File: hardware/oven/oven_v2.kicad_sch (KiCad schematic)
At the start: 21 parts, among them J1 NEUTRAL, J10 SERIAL, J2 5V_IN, J3 RELAY_PWR, J4 LIVE, J5 OUTPUT, J6 RELAY_CTRL, J7 DISPLAY, J8 NUMPAD, J9 AVR-ISP-6, U1 ATmega328-AU, U2 MAX6675, Y1 16M

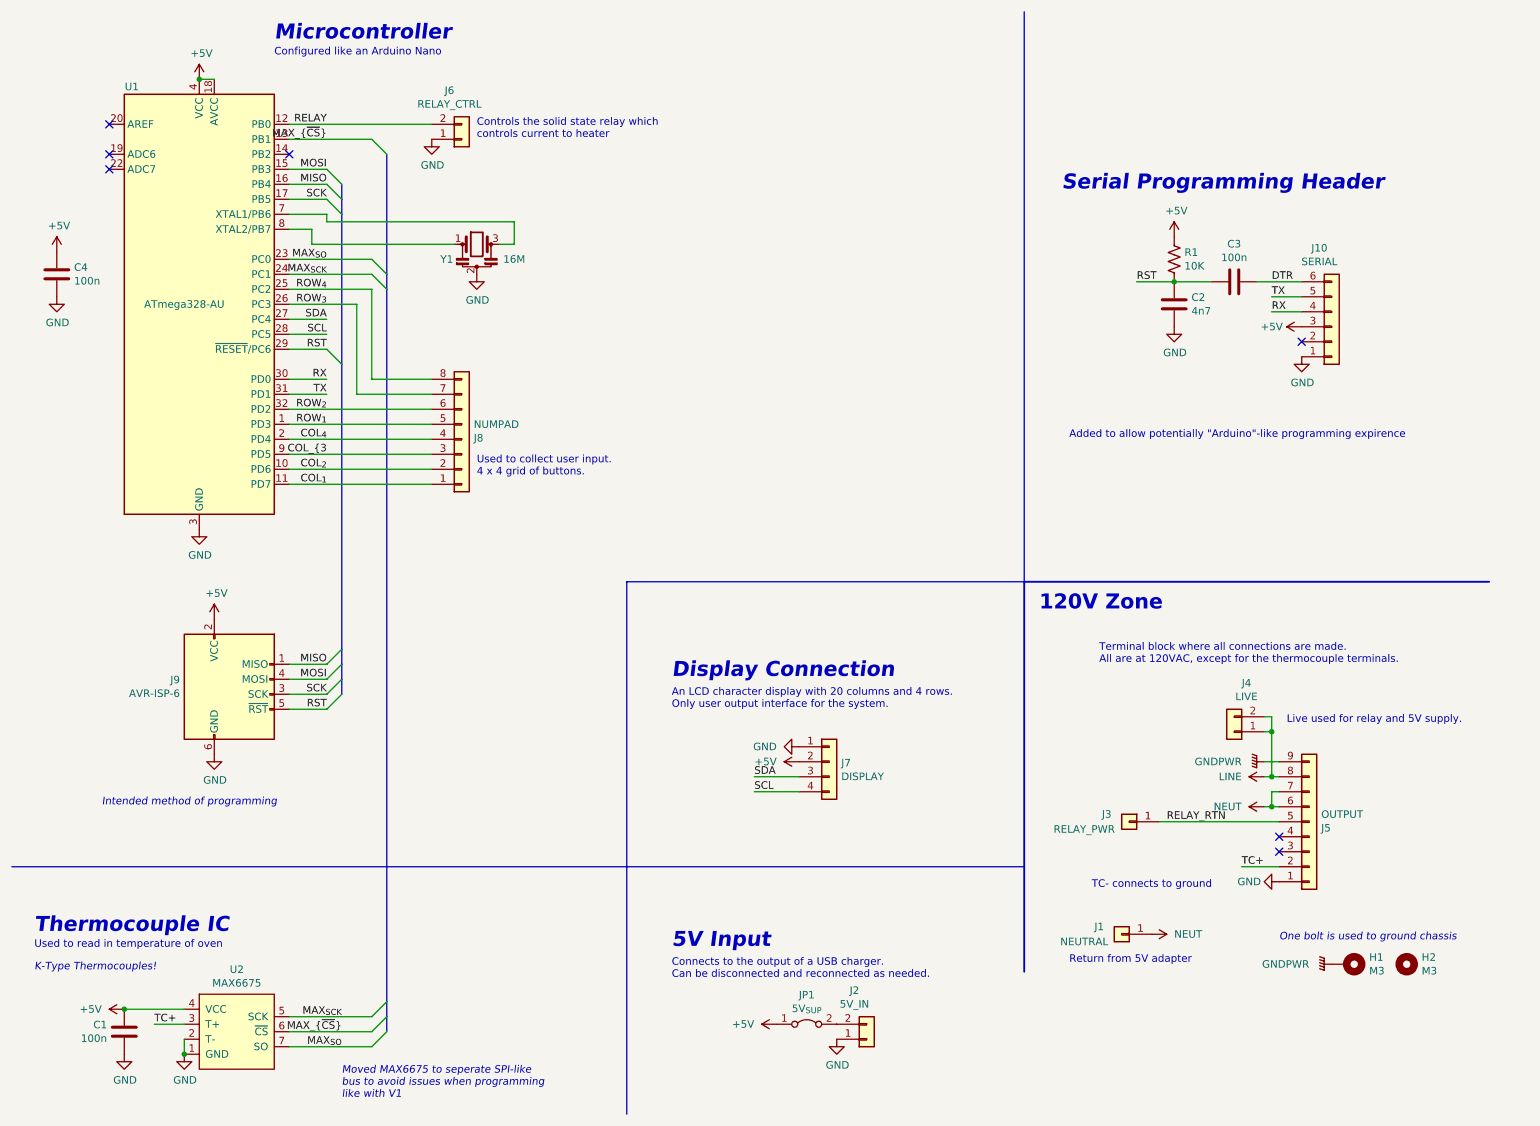
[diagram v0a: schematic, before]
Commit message: Updated oven revision to have buzzer
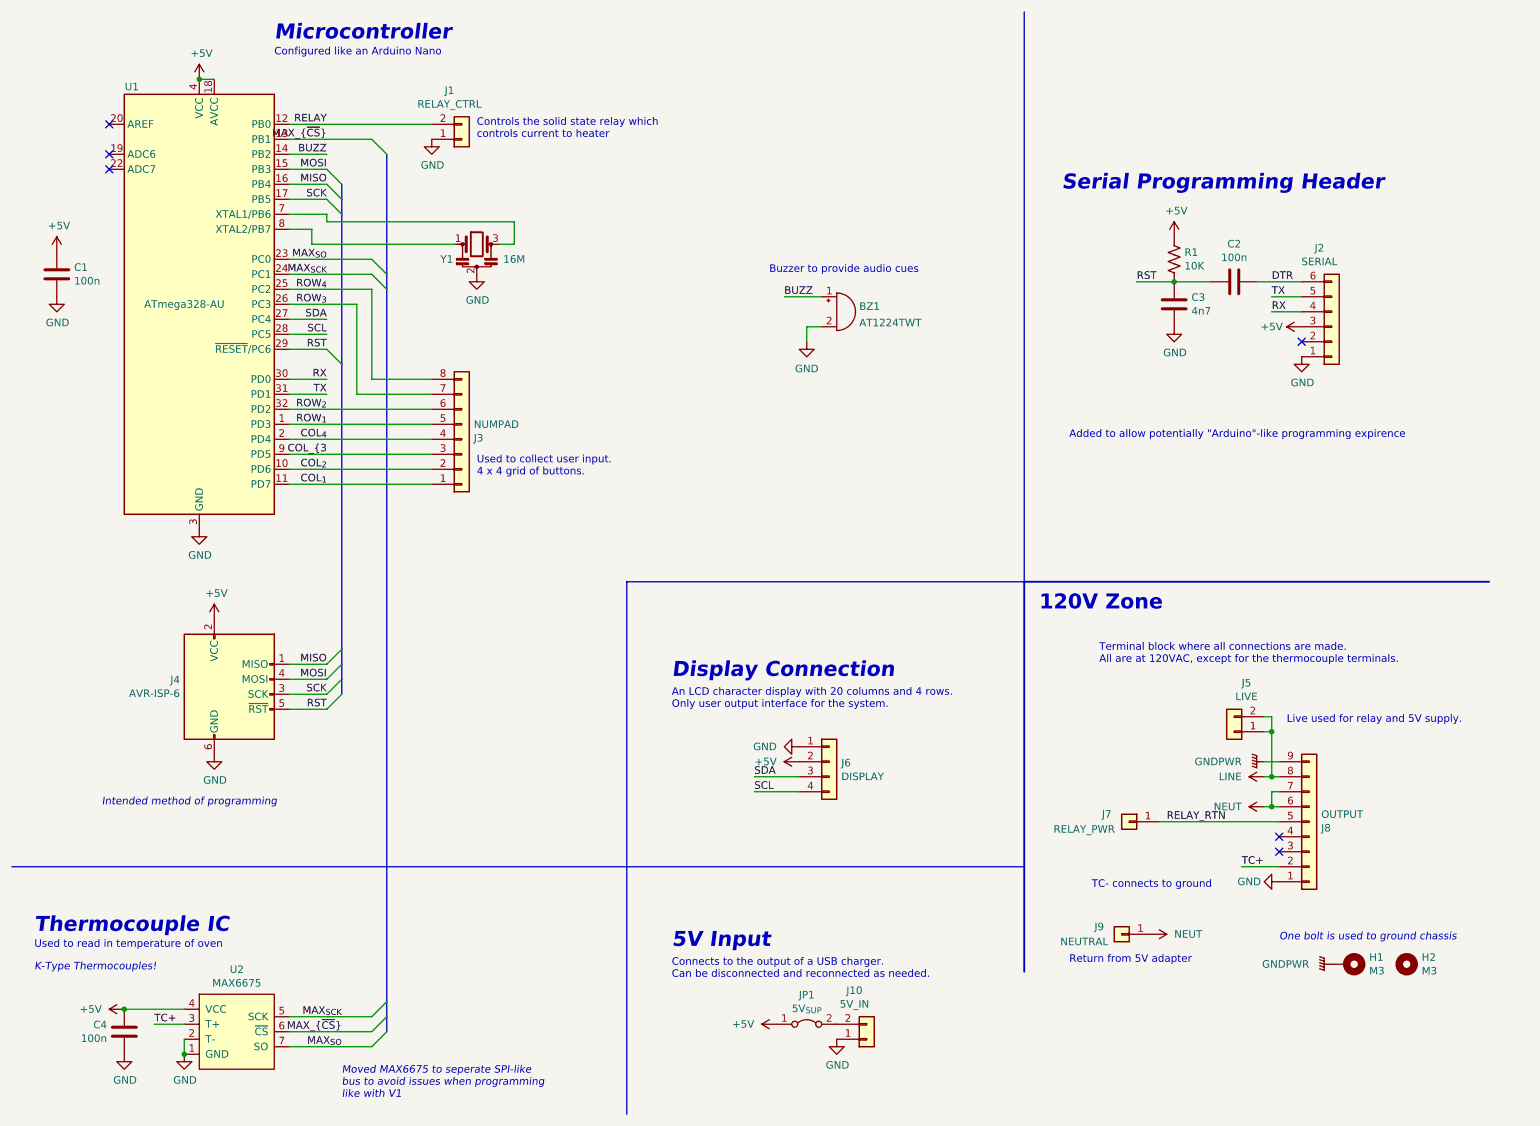
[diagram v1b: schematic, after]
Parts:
- added BZ1: AT1224TWT, Buzzer_Beeper:MagneticBuzzer_ProSignal_ABT-410-RC, symbol Device:Buzzer
- renumbered C4 to C1, C3 to C2, C2 to C3, C1 to C4, J6 to J1, J2 to J10, J10 to J2, J8 to J3, J9 to J4, J4 to J5, J7 to J6, J3 to J7, J5 to J8, J1 to J9
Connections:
- net GND: now also BZ1.2 (+)
- net BUZZ: now reaches U1.14 (PB2)
- net BUZZ: now also BZ1.1 (-)
- no-connect marks 7 -> 6
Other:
- note added: "Buzzer to provide audio cues"
